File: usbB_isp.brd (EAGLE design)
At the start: 100 x 80 mm, 12 parts, among them IC1 788TV, IC2 TINY13-20PU, X1 PN61729-S

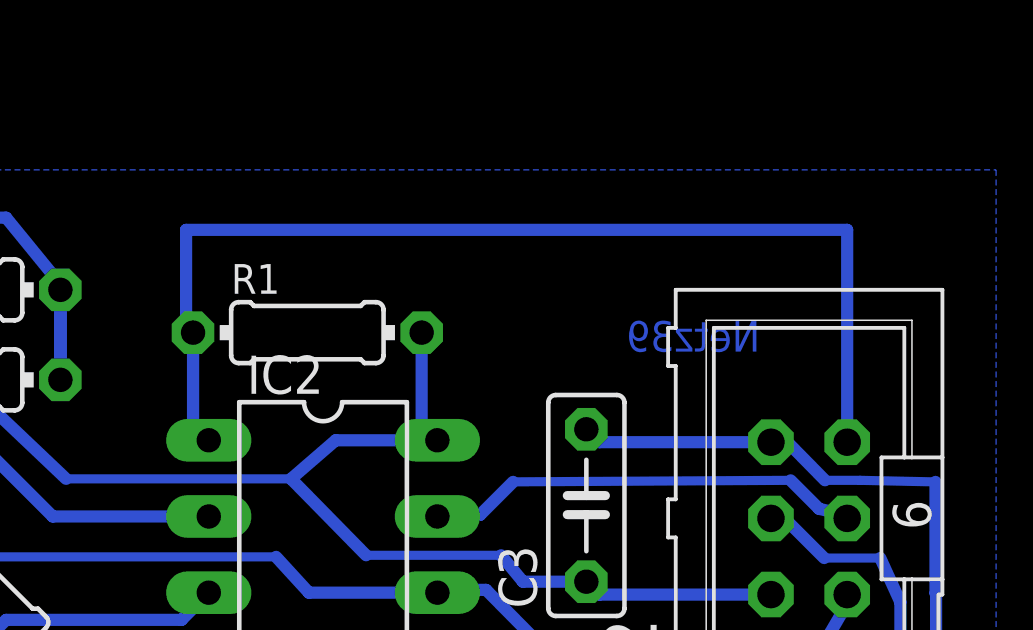
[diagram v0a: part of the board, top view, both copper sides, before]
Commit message: better GND connection
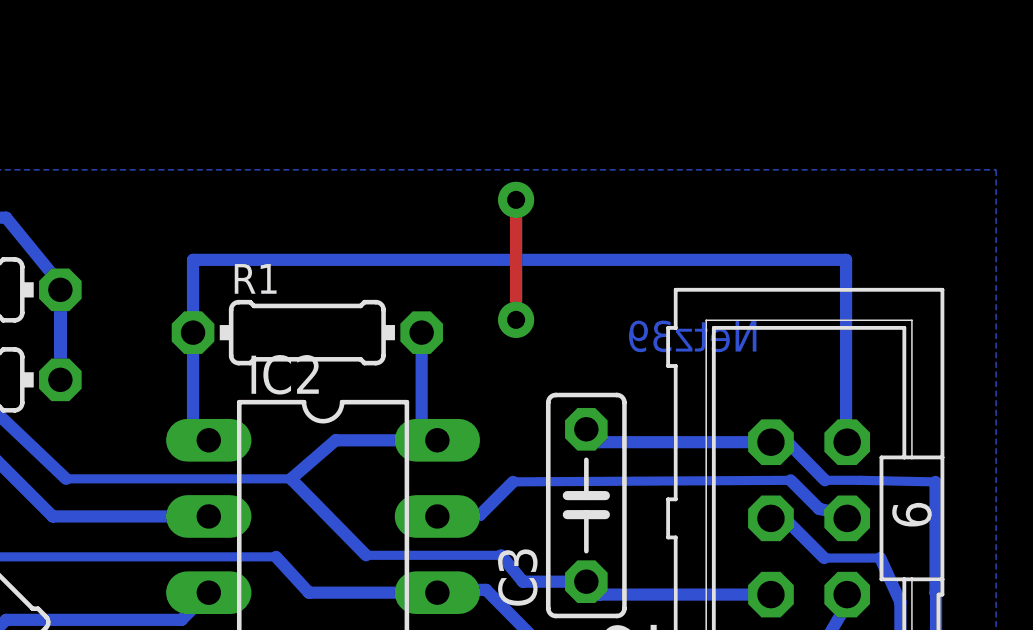
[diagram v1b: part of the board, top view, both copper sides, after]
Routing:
- net GND: track 93.5 -> 97.5 mm, vias 0 -> 2
- net _RESET: track 36.6 -> 34.1 mm
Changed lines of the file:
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@@
 <contactref element="X1" pad="S1"/>
 <contactref element="X1" pad="3"/>
+<via x="59" y="22" extent="1-16" drill="0.6" shape="square"/>
+<via x="59" y="18" extent="1-16" drill="0.6" shape="square"/>
+<wire x1="59" y1="22" x2="59" y2="18" width="0.4064" layer="1"/>
 </signal>
 <signal name="VCC">
@@
 <wire x1="48.232" y1="14.51" x2="48.756" y2="13.986" width="0.4064" layer="16"/>
 <wire x1="70" y1="13.958" x2="70.036" y2="13.922" width="0.4064" layer="16"/>
-<wire x1="48.232" y1="17.574" x2="48" y2="17.574" width="0.4064" layer="16"/>
-<wire x1="48" y1="17.574" x2="48" y2="21" width="0.4064" layer="16"/>
-<wire x1="48" y1="21" x2="70.036" y2="21" width="0.4064" layer="16"/>
-<wire x1="70.036" y1="21" x2="70.036" y2="13.922" width="0.4064" layer="16"/>
+<wire x1="70" y1="13.958" x2="70" y2="20" width="0.4064" layer="16"/>
+<wire x1="70" y1="20" x2="48.232" y2="20" width="0.4064" layer="16"/>
+<wire x1="48.232" y1="20" x2="48.232" y2="17.574" width="0.4064" layer="16"/>
 </signal>
 <signal name="N$6">
